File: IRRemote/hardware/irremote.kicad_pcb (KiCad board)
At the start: 2 copper layers, 68.5 x 32 mm, 41 parts, among them P1 USB_OTG, P2 TL1838_PINHEADER, P3 DS18B20_PINHEADER_TO92, P4 CONN_02X04, P5 CONN_01X04, P6 CONN_01X05, P7 CONN_01X04, P8 TEMP6000, P9 CONN_01X02, Q1 Q_NPN_BEC (MMBT2222ALT1G, 145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

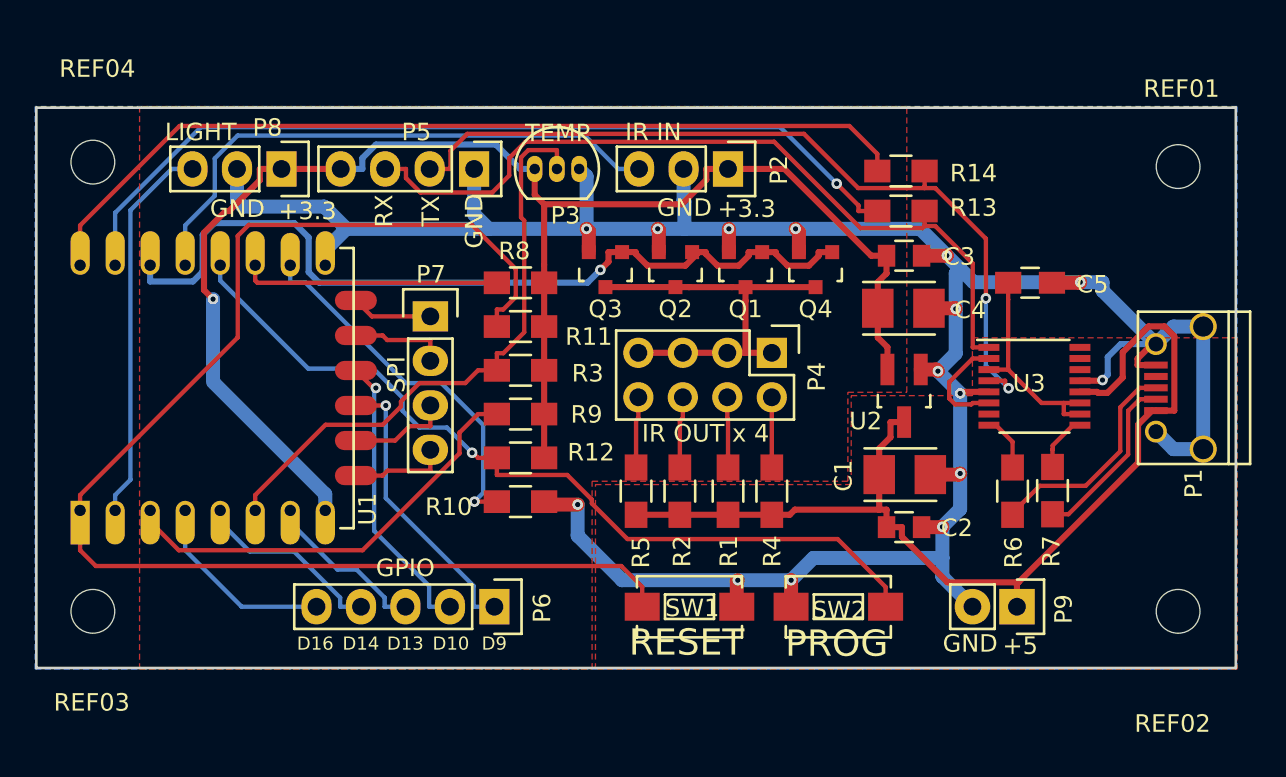
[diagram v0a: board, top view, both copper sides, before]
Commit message: removed the uart and made the board smaller
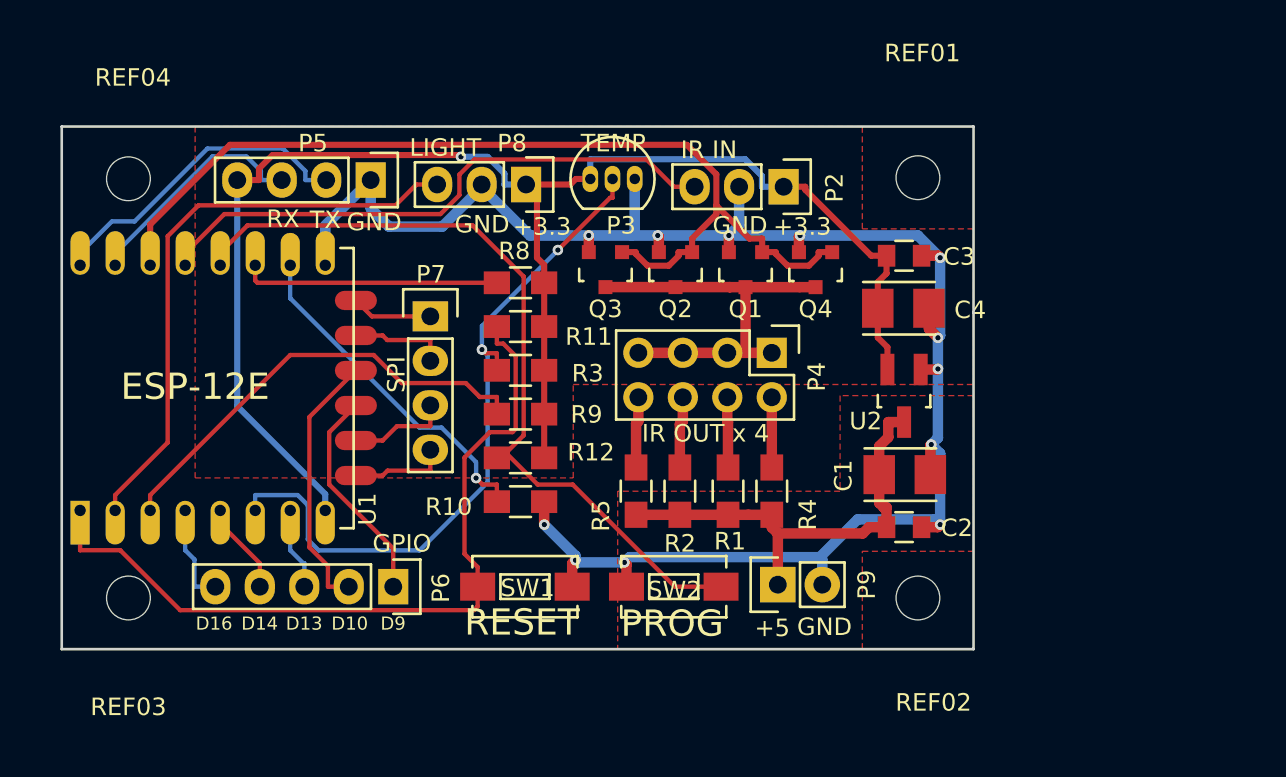
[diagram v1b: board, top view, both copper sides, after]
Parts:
- removed C5: C, Capacitors_SMD:C_0805_HandSoldering
- removed P1: USB_OTG, MyKiCadLibs:USB_Micro-B-OshPark
- removed R13, R14: 470, Resistors_SMD:R_0805_HandSoldering
- removed R6, R7: 27, Resistors_SMD:R_0805_HandSoldering
- removed U3: FT230XS, Housings_SSOP:SSOP-16_3.9x4.9mm_Pitch0.635mm
- moved REF02 14.9 mm to (156.8, 79.5)
- moved REF01 14.9 mm to (156.8, 55.5)
- moved P8 14.0 mm to (134.5, 55.9)
- moved P9 13.7 mm to (148.8, 78.7), turned to 90 degrees
- moved SW1 9.47 mm to (134.4, 78.9)
- moved SW2 9.47 mm to (142.9, 78.9)
- moved P5 5.94 mm to (125.6, 55.6)
- moved P6 5.89 mm to (126.9, 78.9)
- moved P2 3.33 mm to (149.2, 56.0)
- moved P3 3.23 mm to (138.1, 55.6)
- moved REF04 2.24 mm to (111.8, 55.6)
- moved REF03 2.17 mm to (111.8, 79.5)
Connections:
- U1 pad 21: Net-(R13-Pad1) -> TXD_UA_1
- U1 pad 22: Net-(R14-Pad1) -> RXD_UA_1
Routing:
- net GND: track 159.6 -> 106.7 mm, vias 15 -> 12
- net Net-(R14-Pad1): track 51.8 -> 0.00 mm
- net Net-(R13-Pad1): track 50.7 -> 0.00 mm, vias 1 -> 0
- net +5V: track 58.6 -> 25.6 mm
- net TXD_UA_1: track 45.8 -> 13.3 mm
- net Net-(R8-Pad1): track 76.9 -> 45.4 mm
- net RXD_UA_1: track 47.2 -> 18.3 mm, vias 2 -> 0
- net USBDP_1_P: track 12.7 -> 0.00 mm
- net Net-(C5-Pad2): track 12.5 -> 0.00 mm
- net TEMT: track 22.0 -> 33.5 mm
- net USBDM_1_N: track 10.1 -> 0.00 mm
- net LED_DR: track 48.8 -> 56.1 mm, vias 1 -> 0
- net TEMP_READ: track 34.2 -> 40.8 mm, vias 0 -> 2
- net Net-(U3-Pad2): track 6.20 -> 0.00 mm
- net Net-(P6-Pad4): track 11.0 -> 5.29 mm
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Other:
- board size 68.5 x 32 mm -> 52.1 x 29.8 mm
- board text added: "ESP-12E"
